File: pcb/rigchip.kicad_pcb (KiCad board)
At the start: 2 copper layers, 41 x 60.5 mm, 28 parts, among them IC1 TSR1, IC2 CHIPv1_0, J1 POWER, J2 DATA, J3 CONTROL

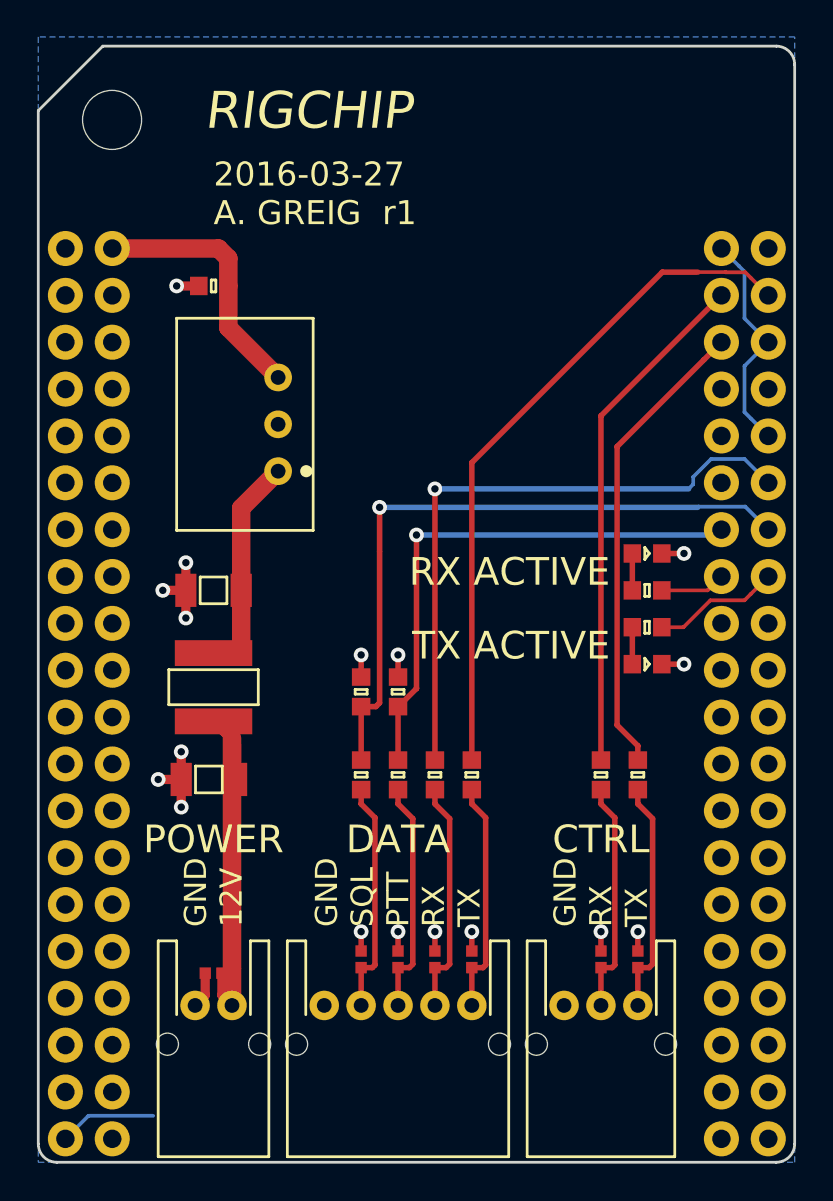
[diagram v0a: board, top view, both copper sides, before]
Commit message: reroute, no more tracks underneath and nice shielding
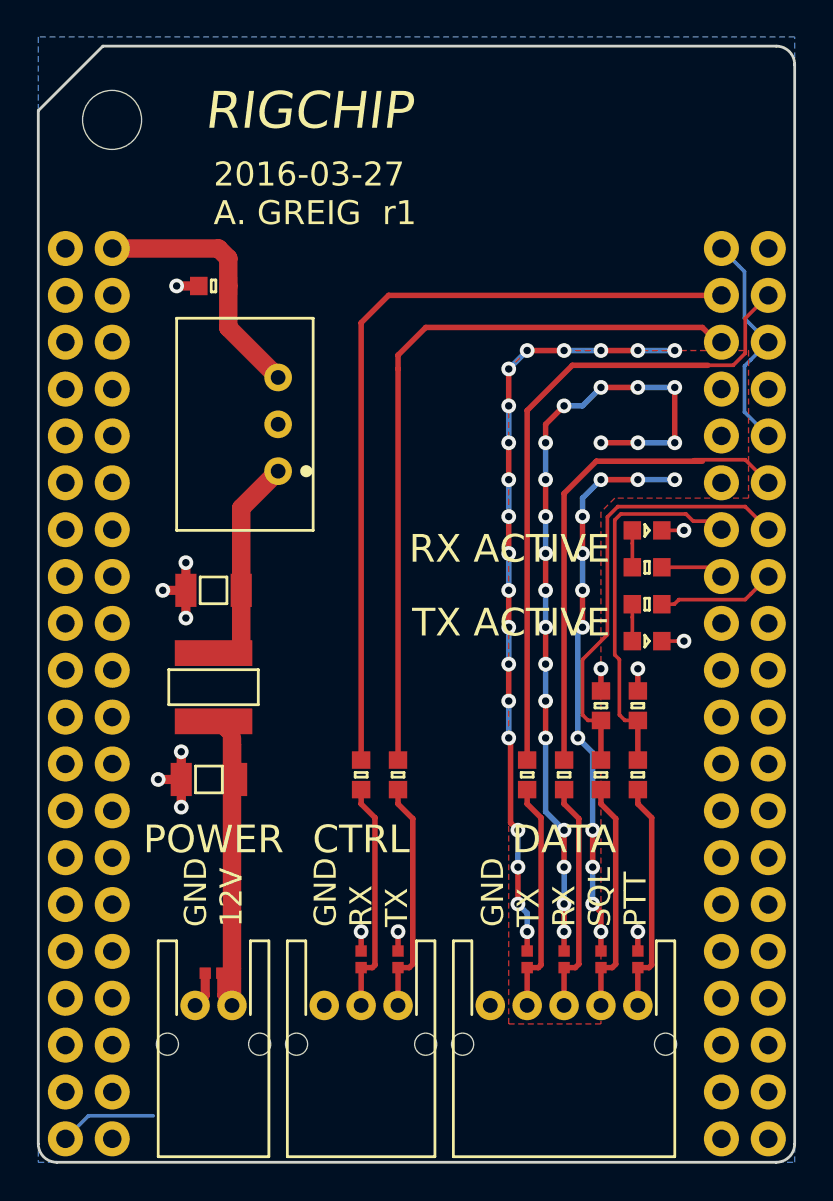
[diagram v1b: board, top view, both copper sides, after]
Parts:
- moved C4 13.0 mm to (80.5, 75.2)
- moved C5 13.0 mm to (82.5, 75.2)
- moved D6 13.0 mm to (67.5, 89.0)
- moved D7 13.0 mm to (69.5, 89.0)
- moved J3 13.0 mm to (67.5, 91.5)
- moved L6 13.0 mm to (69.5, 79.0)
- moved L7 13.0 mm to (67.5, 79.0)
- moved D2 9.00 mm to (76.5, 89.0)
- moved D3 9.00 mm to (78.5, 89.0)
- moved D4 9.00 mm to (80.5, 89.0)
- moved D5 9.00 mm to (82.5, 89.0)
- moved J2 9.00 mm to (78.5, 91.5)
- moved L2 9.00 mm to (82.5, 79.0)
- moved L3 9.00 mm to (80.5, 79.0)
- moved L4 9.00 mm to (78.5, 79.0)
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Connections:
- L2 pad 2: /TX_AUDIO -> /PTT
- L3 pad 2: /RX_AUDIO -> /SQL
- L4 pad 2: /PTT -> /RX_AUDIO
- L5 pad 2: /SQL -> /TX_AUDIO
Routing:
- net GND: track 40.3 -> 152.9 mm, vias 17 -> 66
- net /RIG_RX: track 27.9 -> 43.8 mm
- net /RIG_TX: track 25.5 -> 40.5 mm
- net /SQL: track 36.2 -> 24.1 mm, vias 1 -> 0
- net /PTT: track 29.3 -> 20.2 mm, vias 1 -> 0
- net /RX_AUDIO: track 34.2 -> 27.3 mm, vias 1 -> 0
- net /TX_AUDIO: track 37.0 -> 35.7 mm
- net Net-(IC2-PadR16): track 6.91 -> 6.39 mm
- added copper zone on F.Cu, net GND
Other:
- board text added: "GND TX RX SQL PTT"
- board text removed: "GND SQL PTT RX TX"

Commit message: shrink pcb to header size
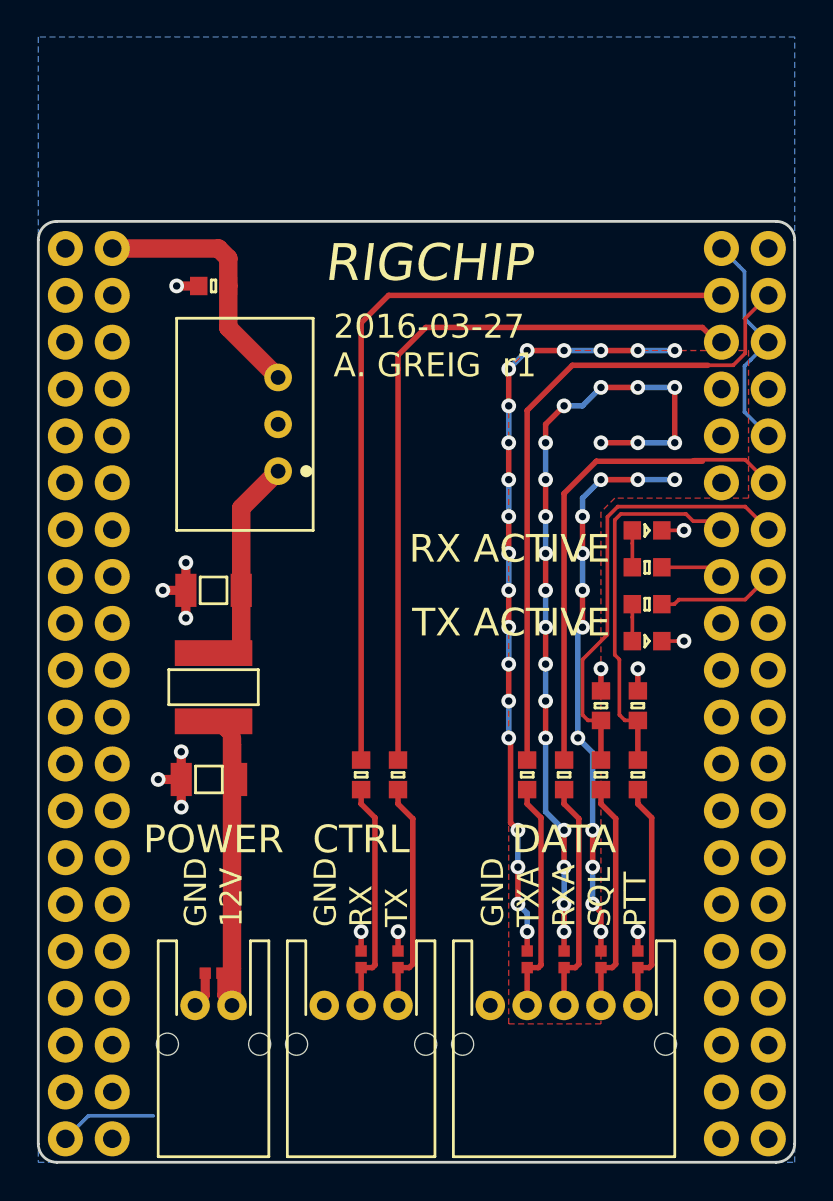
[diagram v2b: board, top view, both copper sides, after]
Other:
- board size 41 x 60.5 mm -> 41 x 51 mm
- board text added: "GND TXA RXA SQL PTT"
- board text removed: "GND TX RX SQL PTT"
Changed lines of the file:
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@@
     (fp_line (start 41 0) (end 41 -60.5) (layer F.Fab) (width 0.01))
     (fp_line (start 0 0) (end 41 0) (layer F.Fab) (width 0.01))
-    (pad "" np_thru_hole circle (at 4 -56.5) (size 3.2 3.2) (drill 3.2) (layers *.Cu *.Mask F.SilkS))
     (pad L39 thru_hole circle (at 1.47 -1.27) (size 1.9 1.9) (drill 1) (layers *.Cu *.Mask F.SilkS)
       (net 2 GND))
@@
       (net 14 "Net-(D9-Pad2)"))
   )
+  (gr_arc (start 51 50) (end 50 50) (angle 90) (layer Edge.Cuts) (width 0.15))
+  (gr_arc (start 90 50) (end 90 49) (angle 90) (layer Edge.Cuts) (width 0.15))
+  (gr_line (start 51 49) (end 90 49) (layer Edge.Cuts) (width 0.15))
   (gr_arc (start 51 99) (end 51 100) (angle 90) (layer Edge.Cuts) (width 0.15))
   (gr_arc (start 90 99) (end 91 99) (angle 90) (layer Edge.Cuts) (width 0.15))
-  (gr_arc (start 90 40.5) (end 90 39.5) (angle 90) (layer Edge.Cuts) (width 0.15))
   (gr_line (start 90 100) (end 51 100) (layer Edge.Cuts) (width 0.15))
-  (gr_line (start 91 40.5) (end 91 99) (layer Edge.Cuts) (width 0.15))
-  (gr_line (start 53.5 39.5) (end 90 39.5) (layer Edge.Cuts) (width 0.15))
-  (gr_line (start 50 43) (end 53.5 39.5) (layer Edge.Cuts) (width 0.15))
-  (gr_line (start 50 99) (end 50 43) (layer Edge.Cuts) (width 0.15))
-  (gr_text "2016-03-27\nA. GREIG  r1" (at 59.5 47.5) (layer F.SilkS)
+  (gr_line (start 91 50) (end 91 99) (layer Edge.Cuts) (width 0.15))
+  (gr_line (start 50 99) (end 50 50) (layer Edge.Cuts) (width 0.15))
+  (gr_text "2016-03-27\nA. GREIG  r1" (at 66 55.75) (layer F.SilkS)
     (effects (font (size 1.3 1.3) (thickness 0.2)) (justify left))
   )
-  (gr_text RIGCHIP (at 59 43) (layer F.SilkS)
+  (gr_text RIGCHIP (at 65.5 51.25) (layer F.SilkS)
     (effects (font (size 2 2) (thickness 0.4) italic) (justify left))
   )
@@
     (effects (font (size 1.5 1.5) (thickness 0.3)))
   )
-  (gr_text "GND\nTX\nRX\nSQL\nPTT" (at 78.5 87.25 90) (layer F.SilkS)
+  (gr_text "GND\nTXA\nRXA\nSQL\nPTT" (at 78.5 87.25 90) (layer F.SilkS)
     (effects (font (size 1.2 1.2) (thickness 0.2)) (justify left))
   )

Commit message: add buffers to cat control
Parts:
- added C6: 100n, agg:0603, F.Cu at (63.5, 79.0)
- added C7: 100n, agg:0603, F.Cu at (69.5, 79.0)
- added IC3: SN74LVC1G07, agg:SOT-23-5, F.Cu at (66.0, 75.0)
- added IC4: SN74LVC1G07, agg:SOT-23-5, F.Cu at (71.0, 75.0)
- added R3: 1k, agg:0603, F.Cu at (65.5, 79.0)
- added R4: 1k, agg:0603, F.Cu at (73.5, 79.0)
- moved L6 2.00 mm to (71.5, 79.0)
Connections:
- IC2 pad L5: Net-(IC2-PadL5) -> 3v3
- IC2 pad R3: /RIG_RX -> /CHIP_TX
- IC2 pad R5: /RIG_TX -> /CHIP_RX
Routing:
- net 3v3: track 0.00 -> 55.4 mm, vias 0 -> 2
- net /CHIP_RX: track 0.00 -> 43.7 mm
- net /CHIP_TX: track 0.00 -> 36.5 mm
- net /RIG_RX: track 43.8 -> 7.48 mm
- net /RIG_TX: track 40.5 -> 4.44 mm
- net 5v: track 14.1 -> 50.0 mm
- net GND: track 152.9 -> 157.6 mm, vias 66 -> 70

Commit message: slight reroute of 3v3 net
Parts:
- moved L6 2.00 mm to (73.5, 79.0)
- moved R4 2.00 mm to (71.5, 79.0)
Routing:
- net /CHIP_RX: track 43.7 -> 38.4 mm
- net Net-(D7-Pad1): track 12.7 -> 13.7 mm
- net 3v3: track 55.4 -> 54.4 mm
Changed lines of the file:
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@@
     (links 73)
     (no_connects 12)
-    (area 38.15 36.645 92.205001 101.625)
+    (area 49.924999 48.924999 91.075001 100.075001)
     (thickness 1.6)
     (drawings 18)
-    (tracks 348)
+    (tracks 349)
     (zones 0)
     (modules 34)
@@
   )
   (module agg:0603 (layer F.Cu)
-    (at 71.5 79 90)
+    (at 73.5 79 90)
     (fp_text reference L6 (at -2.225 0 180) (layer F.Fab)
       (effects (font (size 1 1) (thickness 0.15)))
@@
   )
   (module agg:0603 (layer F.Cu)
-    (at 73.5 79 90)
+    (at 71.5 79 90)
     (fp_text reference R4 (at -2.225 0 180) (layer F.Fab)
       (effects (font (size 1 1) (thickness 0.15)))
@@
   (segment (start 60.3 52.5) (end 60.3 54.76) (width 1) (layer F.Cu) (net 1))
   (segment (start 60.3 54.76) (end 63 57.46) (width 1) (layer F.Cu) (net 1))
+  (segment (start 69.5 79.8) (end 69.5 80.75) (width 0.3) (layer F.Cu) (net 2))
+  (segment (start 69.5 80.75) (end 69.75 81) (width 0.3) (layer F.Cu) (net 2))
+  (via (at 69.75 81) (size 0.8) (drill 0.4) (layers F.Cu B.Cu) (net 2))
   (segment (start 72.3 74.05) (end 72.3 73.2) (width 0.3) (layer F.Cu) (net 2))
   (segment (start 72.3 73.2) (end 72.5 73) (width 0.3) (layer F.Cu) (net 2))
@@
   (segment (start 67.3 73.2) (end 67.5 73) (width 0.3) (layer F.Cu) (net 2))
   (via (at 67.5 73) (size 0.8) (drill 0.4) (layers F.Cu B.Cu) (net 2))
-  (segment (start 69.5 79.8) (end 69.5 81) (width 0.3) (layer F.Cu) (net 2))
-  (via (at 69.5 81) (size 0.8) (drill 0.4) (layers F.Cu B.Cu) (net 2))
   (segment (start 63.5 79.8) (end 63.5 81) (width 0.3) (layer F.Cu) (net 2))
   (via (at 63.5 81) (size 0.8) (drill 0.4) (layers F.Cu B.Cu) (net 2))
@@
   (segment (start 82.5 80.575) (end 82.5 79.8) (width 0.3) (layer F.Cu) (net 10))
   (segment (start 82.5 91.5) (end 82.5 89.45) (width 0.3) (layer F.Cu) (net 10))
-  (segment (start 67.5 89.45) (end 68.11 89.45) (width 0.3) (layer F.Cu) (net 11))
-  (segment (start 68.11 89.45) (end 68.250001 89.309999) (width 0.3) (layer F.Cu) (net 11))
-  (segment (start 68.250001 81.325001) (end 67.5 80.575) (width 0.3) (layer F.Cu) (net 11))
-  (segment (start 67.5 80.575) (end 67.5 79.8) (width 0.3) (layer F.Cu) (net 11))
-  (segment (start 68.250001 89.309999) (end 68.250001 81.325001) (width 0.3) (layer F.Cu) (net 11))
+  (segment (start 67.5 79.8) (end 67.5 85.75) (width 0.3) (layer F.Cu) (net 11))
+  (segment (start 67.5 85.75) (end 68.5 86.75) (width 0.3) (layer F.Cu) (net 11))
+  (segment (start 68.5 86.75) (end 68.5 89.06) (width 0.3) (layer F.Cu) (net 11))
+  (segment (start 68.5 89.06) (end 68.11 89.45) (width 0.3) (layer F.Cu) (net 11))
+  (segment (start 68.11 89.45) (end 67.5 89.45) (width 0.3) (layer F.Cu) (net 11))
   (segment (start 67.5 91.5) (end 67.5 89.45) (width 0.3) (layer F.Cu) (net 11))
-  (segment (start 71.5 79.8) (end 71.5 80.575) (width 0.3) (layer F.Cu) (net 12))
-  (segment (start 71.5 80.575) (end 70.3 81.775) (width 0.3) (layer F.Cu) (net 12))
-  (segment (start 70.3 81.775) (end 70.3 89.000002) (width 0.3) (layer F.Cu) (net 12))
-  (segment (start 70.3 89.000002) (end 69.850002 89.45) (width 0.3) (layer F.Cu) (net 12))
-  (segment (start 69.850002 89.45) (end 69.5 89.45) (width 0.3) (layer F.Cu) (net 12))
+  (segment (start 73.5 83.75) (end 73.5 79.8) (width 0.3) (layer F.Cu) (net 12))
+  (segment (start 70.5 86.75) (end 73.5 83.75) (width 0.3) (layer F.Cu) (net 12))
+  (segment (start 70.5 89.06) (end 70.5 86.75) (width 0.3) (layer F.Cu) (net 12))
+  (segment (start 69.5 89.45) (end 70.11 89.45) (width 0.3) (layer F.Cu) (net 12))
+  (segment (start 70.11 89.45) (end 70.5 89.06) (width 0.3) (layer F.Cu) (net 12))
   (segment (start 69.5 91.5) (end 69.5 89.45) (width 0.3) (layer F.Cu) (net 12))
   (segment (start 82.2 65.75) (end 82.2 66.45) (width 0.2) (layer F.Cu) (net 13))
@@
   (segment (start 78.5 63.75) (end 80.25 62) (width 0.3) (layer F.Cu) (net 72))
   (segment (start 78.5 78.2) (end 78.5 63.75) (width 0.3) (layer F.Cu) (net 72))
-  (segment (start 71 75.45) (end 71 76.925) (width 0.3) (layer F.Cu) (net 76))
-  (segment (start 71 76.925) (end 71.5 77.425) (width 0.3) (layer F.Cu) (net 76))
-  (segment (start 71.5 77.425) (end 71.5 78.2) (width 0.3) (layer F.Cu) (net 76))
-  (segment (start 72.3 75) (end 71.45 75) (width 0.3) (layer F.Cu) (net 76))
-  (segment (start 71.45 75) (end 71 75.45) (width 0.3) (layer F.Cu) (net 76))
+  (segment (start 72.3 75) (end 73.15 75) (width 0.3) (layer F.Cu) (net 76))
+  (segment (start 73.15 75) (end 73.5 75.35) (width 0.3) (layer F.Cu) (net 76))
+  (segment (start 73.5 75.35) (end 73.5 77.425) (width 0.3) (layer F.Cu) (net 76))
+  (segment (start 73.5 77.425) (end 73.5 78.2) (width 0.3) (layer F.Cu) (net 76))
   (segment (start 65.5 78.2) (end 66.5 78.2) (width 0.3) (layer F.Cu) (net 77))
   (segment (start 65.699999 74.05) (end 66.399999 74.75) (width 0.3) (layer F.Cu) (net 77))
@@
   (segment (start 88.319999 56.150001) (end 87.669999 56.800001) (width 0.2) (layer F.Cu) (net 78))
   (segment (start 76.5 78.2) (end 76.5 59.25) (width 0.3) (layer F.Cu) (net 78))
-  (segment (start 72.5 81) (end 72.5 80.8) (width 0.3) (layer F.Cu) (net 80))
-  (segment (start 72.5 80.8) (end 73.5 79.8) (width 0.3) (layer F.Cu) (net 80))
-  (segment (start 67.5 82) (end 71.5 82) (width 0.3) (layer B.Cu) (net 80))
-  (segment (start 71.5 82) (end 72.5 81) (width 0.3) (layer B.Cu) (net 80))
-  (via (at 72.5 81) (size 0.8) (drill 0.4) (layers F.Cu B.Cu) (net 80))
-  (segment (start 66.5 81) (end 67.5 82) (width 0.3) (layer B.Cu) (net 80))
-  (segment (start 62.5 81.5) (end 63 82) (width 0.3) (layer F.Cu) (net 80))
+  (segment (start 70.75 82) (end 71.5 81.25) (width 0.3) (layer F.Cu) (net 80))
+  (segment (start 71.5 81.25) (end 71.5 79.8) (width 0.3) (layer F.Cu) (net 80))
+  (segment (start 68.934315 82) (end 70.75 82) (width 0.3) (layer F.Cu) (net 80))
+  (segment (start 68.5 81) (end 68.5 81.565685) (width 0.3) (layer F.Cu) (net 80))
+  (segment (start 68.5 81.565685) (end 68.934315 82) (width 0.3) (layer F.Cu) (net 80))
+  (segment (start 66.5 81) (end 68.5 81) (width 0.3) (layer B.Cu) (net 80))
+  (via (at 68.5 81) (size 0.8) (drill 0.4) (layers F.Cu B.Cu) (net 80))
   (segment (start 63 82) (end 65.5 82) (width 0.3) (layer F.Cu) (net 80))
   (segment (start 65.5 82) (end 66.5 81) (width 0.3) (layer F.Cu) (net 80))
   (via (at 66.5 81) (size 0.8) (drill 0.4) (layers F.Cu B.Cu) (net 80))
+  (segment (start 62.5 81.5) (end 63 82) (width 0.3) (layer F.Cu) (net 80))
   (segment (start 62.5 81.25) (end 62.5 81.5) (width 0.3) (layer F.Cu) (net 80))
   (segment (start 62.5 72.75) (end 62.5 78.25) (width 0.3) (layer F.Cu) (net 80))
@@
   (segment (start 63.5 78.2) (end 63.5 76.3) (width 0.3) (layer F.Cu) (net 80))
   (segment (start 63.85 75.95) (end 64.7 75.95) (width 0.3) (layer F.Cu) (net 80))
-  (segment (start 69.7 71.75) (end 73 71.75) (width 0.3) (layer F.Cu) (net 81))
-  (segment (start 73 71.75) (end 74 72.75) (width 0.3) (layer F.Cu) (net 81))
-  (segment (start 74 72.75) (end 74 77.7) (width 0.3) (layer F.Cu) (net 81))
-  (segment (start 74 77.7) (end 73.5 78.2) (width 0.3) (layer F.Cu) (net 81))
+  (segment (start 69.7 74.05) (end 69.95 74.05) (width 0.3) (layer F.Cu) (net 81))
+  (segment (start 69.95 74.05) (end 71 75.1) (width 0.3) (layer F.Cu) (net 81))
+  (segment (start 71 75.1) (end 71 77.7) (width 0.3) (layer F.Cu) (net 81))
+  (segment (start 71 77.7) (end 71.5 78.2) (width 0.3) (layer F.Cu) (net 81))
   (segment (start 69.7 71.75) (end 69.7 61.689998) (width 0.3) (layer F.Cu) (net 81))
   (segment (start 69.7 74.05) (end 69.7 71.75) (width 0.3) (layer F.Cu) (net 81))
